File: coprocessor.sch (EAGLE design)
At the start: 49 parts, among them IC1 MEGA32U2, J1 AVR_SPI_PRG_6NS, U1 TPS61090RSAR, U3 V_REG_LDOSMD2, U4 AZV321, U5 MCP48, U6 16MHZ, U7 CBT3244AD

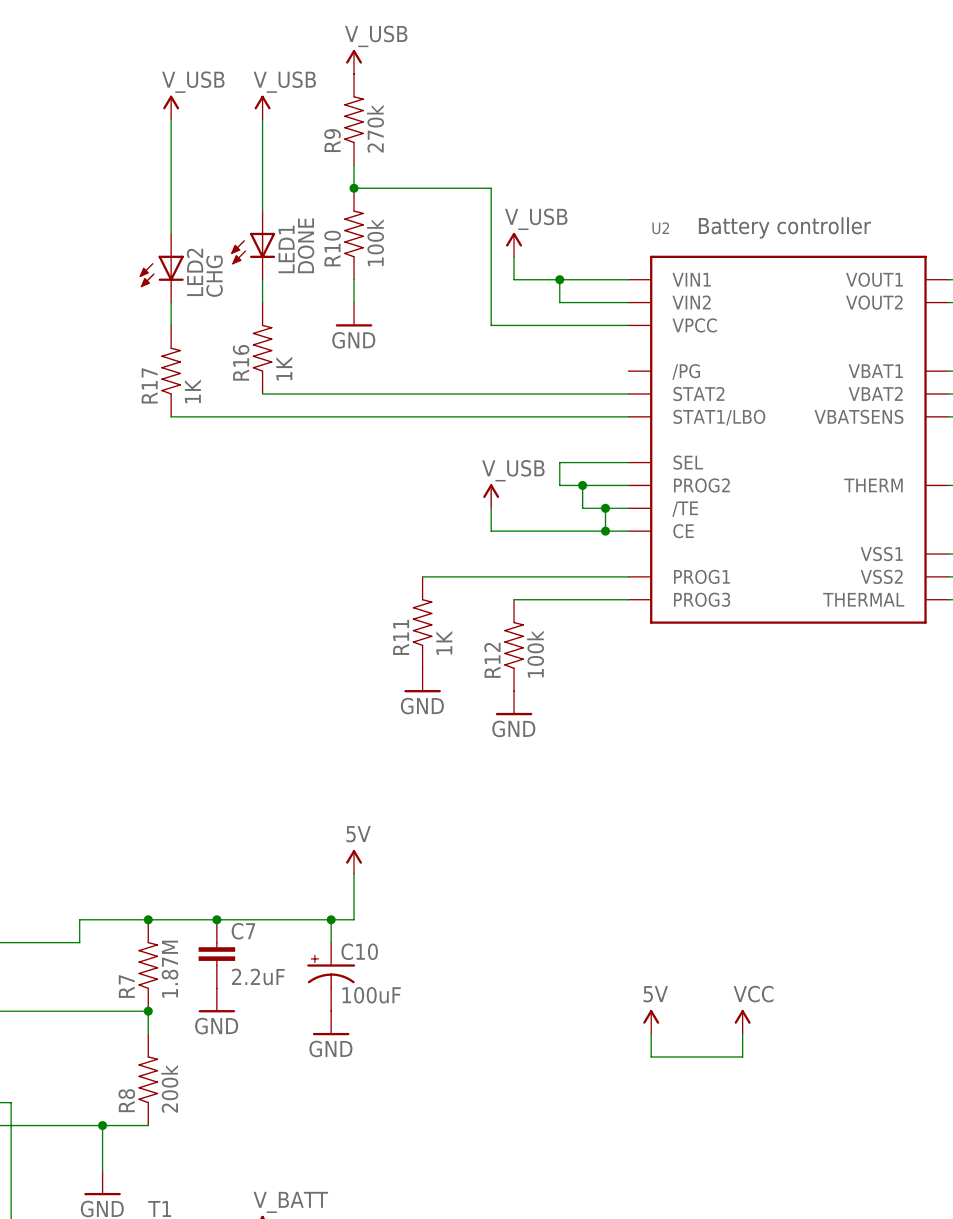
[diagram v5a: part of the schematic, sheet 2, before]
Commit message: redid the inductor to save some space
I noticed that I setup the charging circuit incorrectly
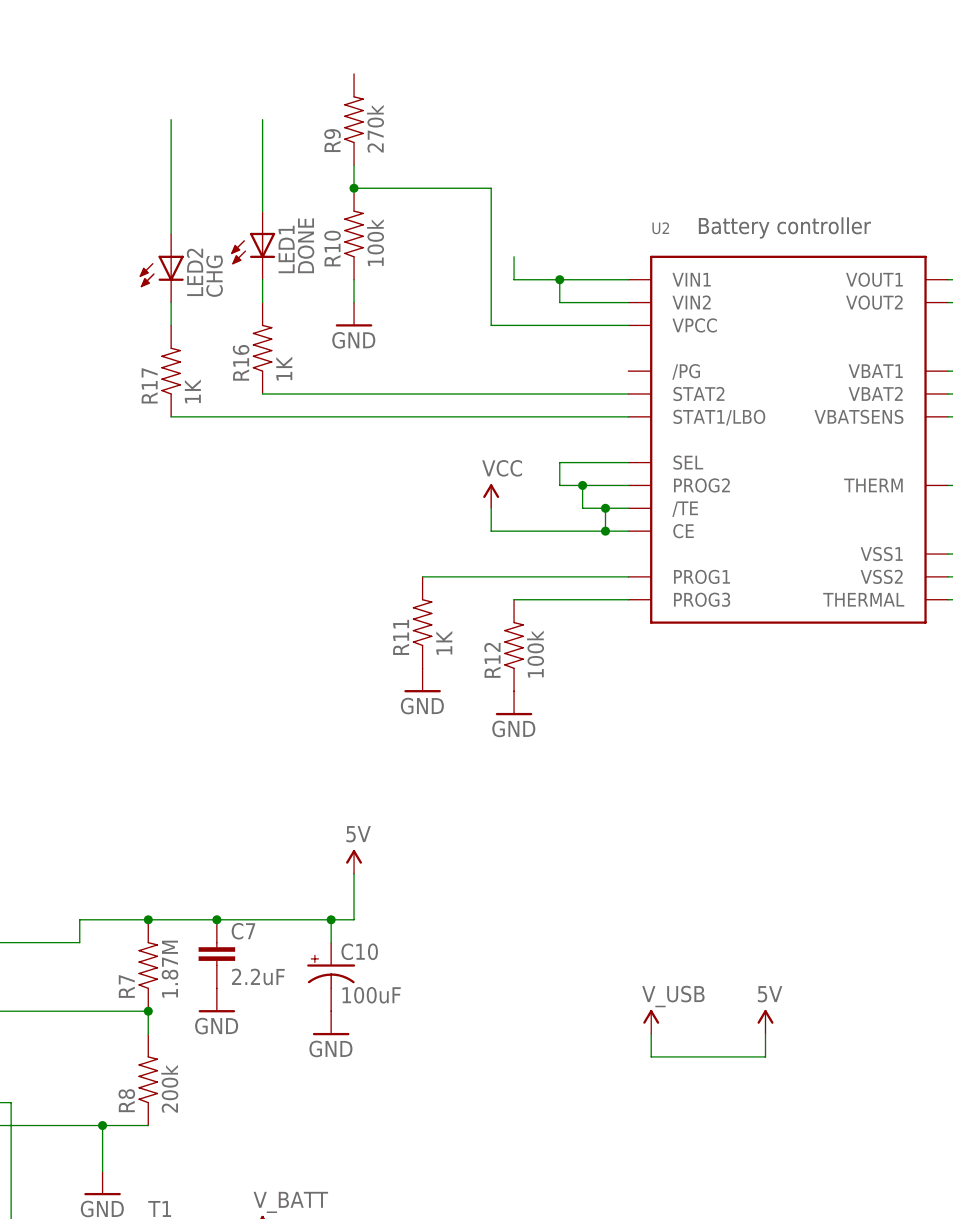
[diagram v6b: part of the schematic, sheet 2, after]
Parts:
- L1: device custom:MICROBUILDER_INDUCTORNR5040 -> custom:MICROBUILDER_INDUCTOR4.9X4.9MM
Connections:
- new net N$31: LED2.A
- new net N$32: LED1.A
- new net N$33: U2.VIN1, U2.VIN2
- net VCC: now also U2./TE, U2.CE, U2.PROG2, U2.SEL
- net V_USB: no longer LED1.A, LED2.A, R9.2, U2./TE, U2.CE, U2.PROG2, U2.SEL, U2.VIN1, U2.VIN2

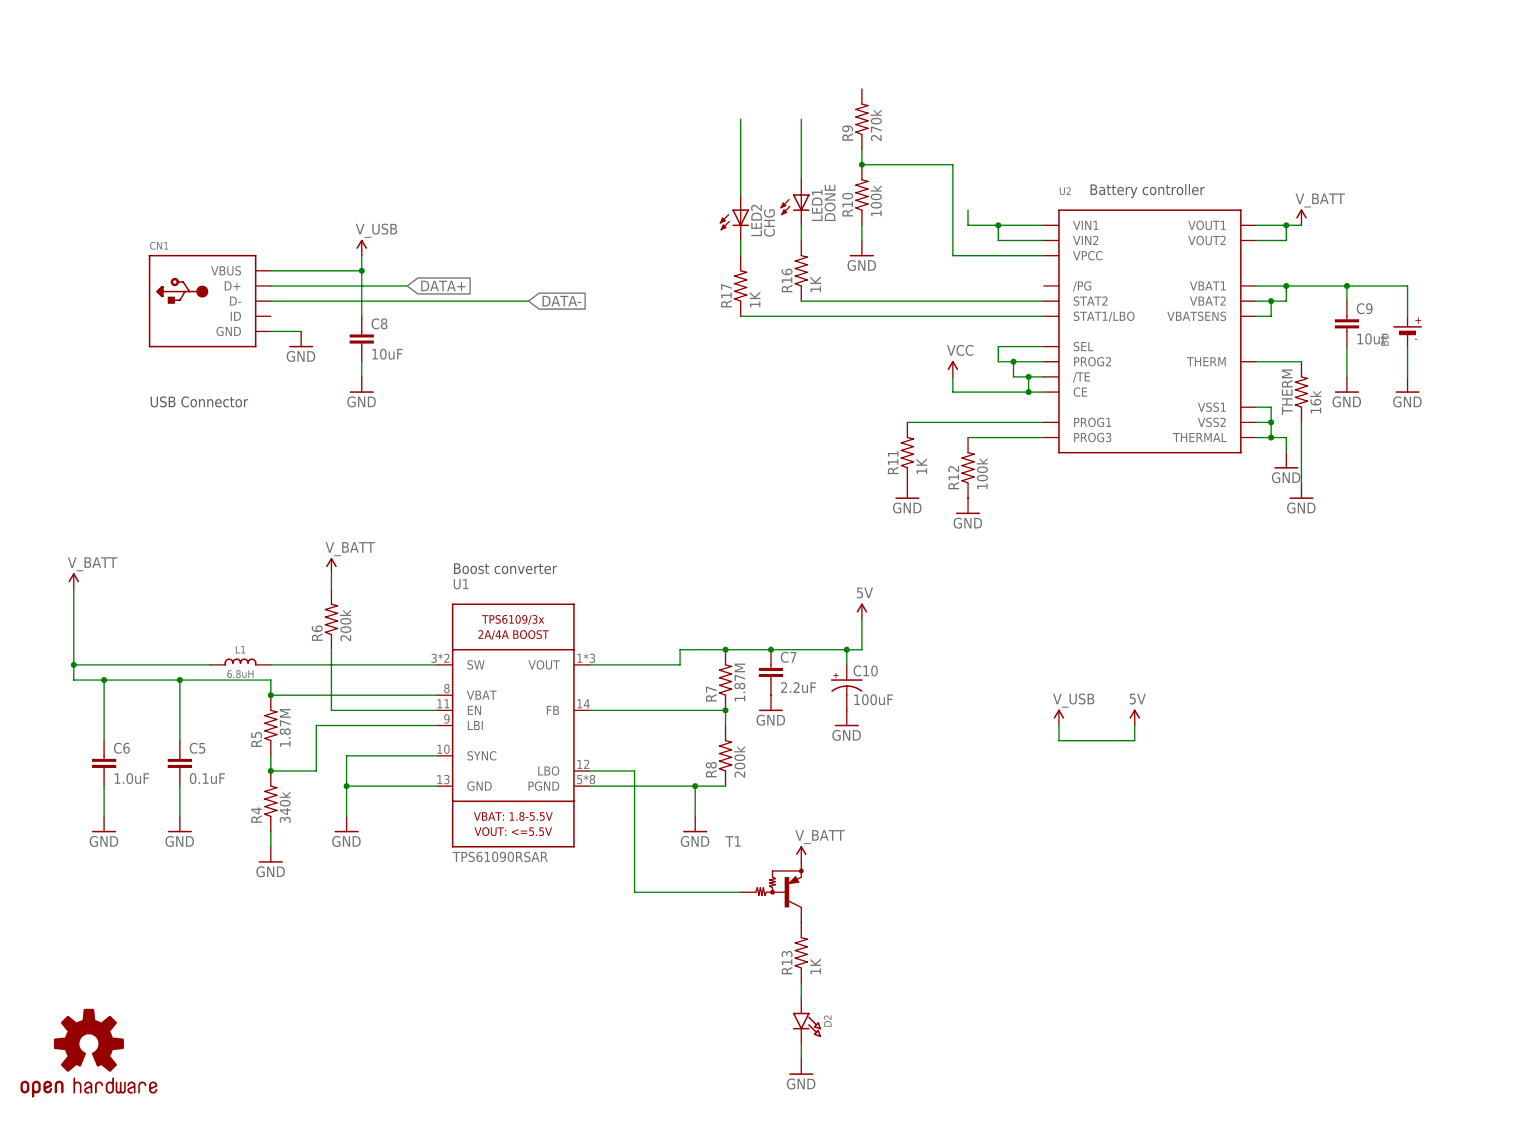
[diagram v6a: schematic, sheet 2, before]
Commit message: had to just completely revamp the voltages
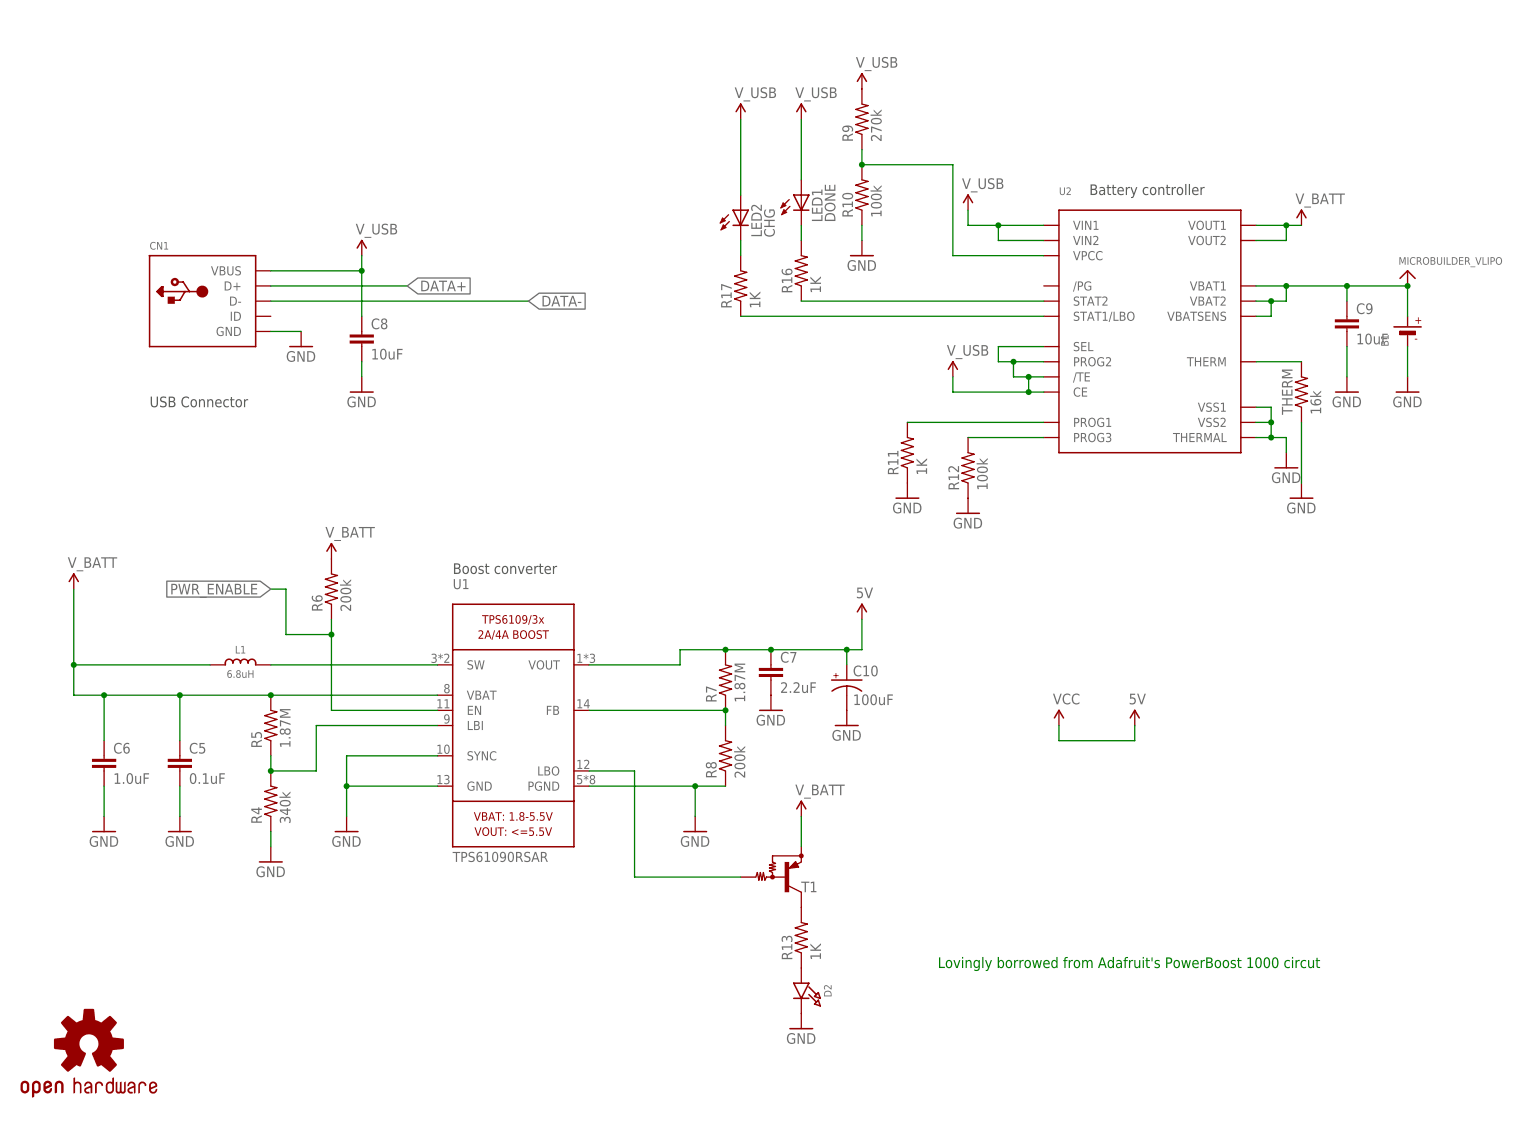
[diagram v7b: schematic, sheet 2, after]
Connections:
- net N$4 renamed PWR_ENABLE
- net N$8 renamed VLIPO
- removed net N$31: LED2.A
- removed net N$32: LED1.A
- removed net N$33: U2.VIN1, U2.VIN2
- net VCC: no longer U2./TE, U2.CE, U2.PROG2, U2.SEL
- net V_USB: now also LED1.A, LED2.A, R9.2, U2./TE, U2.CE, U2.PROG2, U2.SEL, U2.VIN1, U2.VIN2
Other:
- note added: "Lovingly borrowed from Adafruit's PowerBoost 1000 circut"
- moved on the sheet: D2, R13, R6, T1

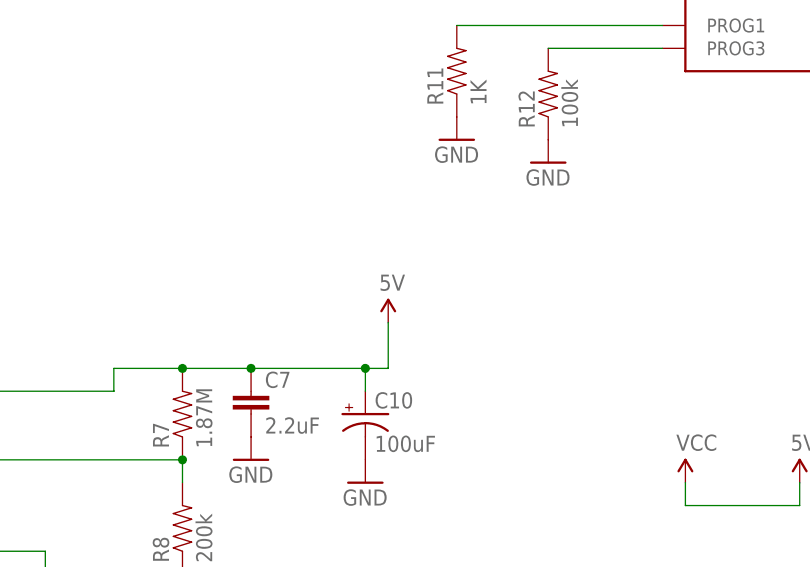
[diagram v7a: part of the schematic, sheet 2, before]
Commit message: added an SVG logo and redid the gerbers
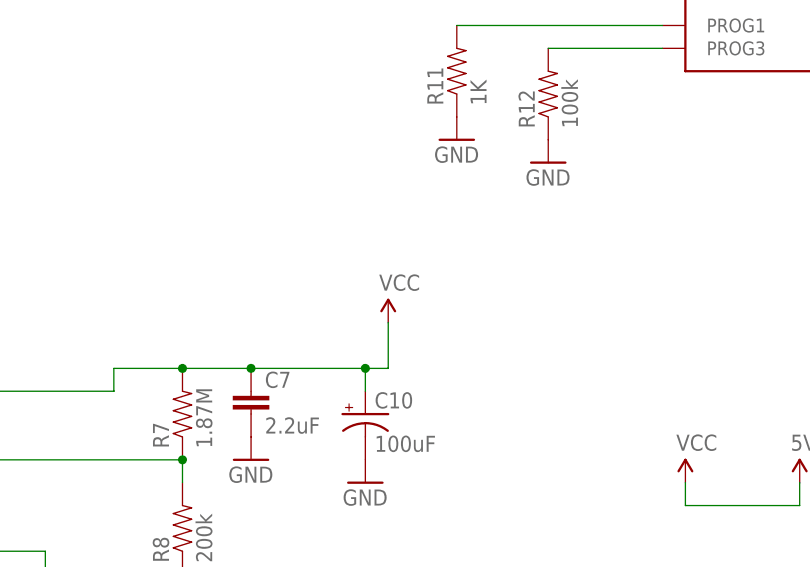
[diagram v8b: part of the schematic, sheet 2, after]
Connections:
- removed net 5V: C10.+, C7.1, R7.2, U1.VOUT
- net VCC: now also C10.+, C7.1, R7.2, U1.VOUT
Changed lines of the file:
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@@
 <part name="GND14" library="SparkFun-Aesthetics" deviceset="GND" device=""/>
 <part name="GND15" library="SparkFun-Aesthetics" deviceset="GND" device=""/>
-<part name="SUPPLY10" library="SparkFun-Aesthetics" deviceset="5V" device=""/>
 <part name="R7" library="SparkFun-Resistors" deviceset="1.8KOHM1/10W1%(0603)" device="" value="1.87M"/>
 <part name="R8" library="SparkFun-Resistors" deviceset="200KOHM1/10W1%(0603)" device="200K" value="200k"/>
@@
 <part name="SUPPLY19" library="SparkFun-Aesthetics" deviceset="V_USB" device=""/>
 <part name="SUPPLY24" library="SparkFun-Aesthetics" deviceset="V_USB" device=""/>
+<part name="SUPPLY10" library="SparkFun-Aesthetics" deviceset="VCC" device=""/>
 </parts>
 <sheets>
@@
 <instance part="GND14" gate="1" x="157.48" y="76.2"/>
 <instance part="GND15" gate="1" x="86.36" y="71.12"/>
-<instance part="SUPPLY10" gate="G$1" x="185.42" y="111.76"/>
 <instance part="R7" gate="G$1" x="162.56" y="101.6" rot="R90"/>
 <instance part="R8" gate="G$1" x="162.56" y="88.9" rot="R90"/>
@@
 <instance part="SUPPLY19" gate="G$1" x="203.2" y="180.34"/>
 <instance part="SUPPLY24" gate="G$1" x="200.66" y="152.4"/>
+<instance part="SUPPLY10" gate="G$1" x="185.42" y="111.76"/>
 </instances>
 <busses>
@@
 <wire x1="86.36" y1="104.14" x2="114.3" y2="104.14" width="0.1524" layer="91"/>
 <pinref part="U1" gate="G$1" pin="SW"/>
-</segment>
-</net>
-<net name="5V" class="0">
-<segment>
-<pinref part="SUPPLY10" gate="G$1" pin="5V"/>
-<wire x1="162.56" y1="106.68" x2="170.18" y2="106.68" width="0.1524" layer="91"/>
-<wire x1="170.18" y1="106.68" x2="182.88" y2="106.68" width="0.1524" layer="91"/>
-<wire x1="182.88" y1="106.68" x2="185.42" y2="106.68" width="0.1524" layer="91"/>
-<wire x1="185.42" y1="106.68" x2="185.42" y2="111.76" width="0.1524" layer="91"/>
-<pinref part="R7" gate="G$1" pin="2"/>
-<pinref part="C7" gate="G$1" pin="1"/>
-<junction x="170.18" y="106.68"/>
-<pinref part="U1" gate="G$1" pin="VOUT"/>
-<wire x1="139.7" y1="104.14" x2="154.94" y2="104.14" width="0.1524" layer="91"/>
-<wire x1="154.94" y1="104.14" x2="154.94" y2="106.68" width="0.1524" layer="91"/>
-<wire x1="154.94" y1="106.68" x2="162.56" y2="106.68" width="0.1524" layer="91"/>
-<junction x="162.56" y="106.68"/>
-<pinref part="C10" gate="G$1" pin="+"/>
-<wire x1="182.88" y1="104.14" x2="182.88" y2="106.68" width="0.1524" layer="91"/>
-<junction x="182.88" y="106.68"/>
 </segment>
 </net>
@@
 <net name="VCC" class="0">
 <segment>
+<pinref part="SUPPLY11" gate="G$1" pin="VCC"/>
 <wire x1="218.44" y1="93.98" x2="218.44" y2="91.44" width="0.1524" layer="91"/>
-<wire x1="218.44" y1="91.44" x2="231.14" y2="91.44" width="0.1524" layer="91"/>
 <pinref part="SUPPLY17" gate="G$1" pin="5V"/>
 <wire x1="231.14" y1="91.44" x2="231.14" y2="93.98" width="0.1524" layer="91"/>
-<pinref part="SUPPLY11" gate="G$1" pin="VCC"/>
-</segment>
-</net>
+<wire x1="218.44" y1="91.44" x2="231.14" y2="91.44" width="0.1524" layer="91"/>
+</segment>
+<segment>
+<wire x1="162.56" y1="106.68" x2="170.18" y2="106.68" width="0.1524" layer="91"/>
+<wire x1="170.18" y1="106.68" x2="182.88" y2="106.68" width="0.1524" layer="91"/>
+<wire x1="182.88" y1="106.68" x2="185.42" y2="106.68" width="0.1524" layer="91"/>
+<pinref part="R7" gate="G$1" pin="2"/>
+<pinref part="C7" gate="G$1" pin="1"/>
+<junction x="170.18" y="106.68"/>
+<pinref part="U1" gate="G$1" pin="VOUT"/>
+<wire x1="139.7" y1="104.14" x2="154.94" y2="104.14" width="0.1524" layer="91"/>
+<wire x1="154.94" y1="104.14" x2="154.94" y2="106.68" width="0.1524" layer="91"/>
+<wire x1="154.94" y1="106.68" x2="162.56" y2="106.68" width="0.1524" layer="91"/>
+<junction x="162.56" y="106.68"/>
+<pinref part="C10" gate="G$1" pin="+"/>
+<wire x1="182.88" y1="104.14" x2="182.88" y2="106.68" width="0.1524" layer="91"/>
+<junction x="182.88" y="106.68"/>
+<wire x1="185.42" y1="106.68" x2="185.42" y2="111.76" width="0.1524" layer="91"/>
+<pinref part="SUPPLY10" gate="G$1" pin="VCC"/>
+</segment>
+</net>
